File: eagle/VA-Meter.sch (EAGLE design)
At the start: 23 parts, among them IC1 MEGA328P, IC2 7805TV

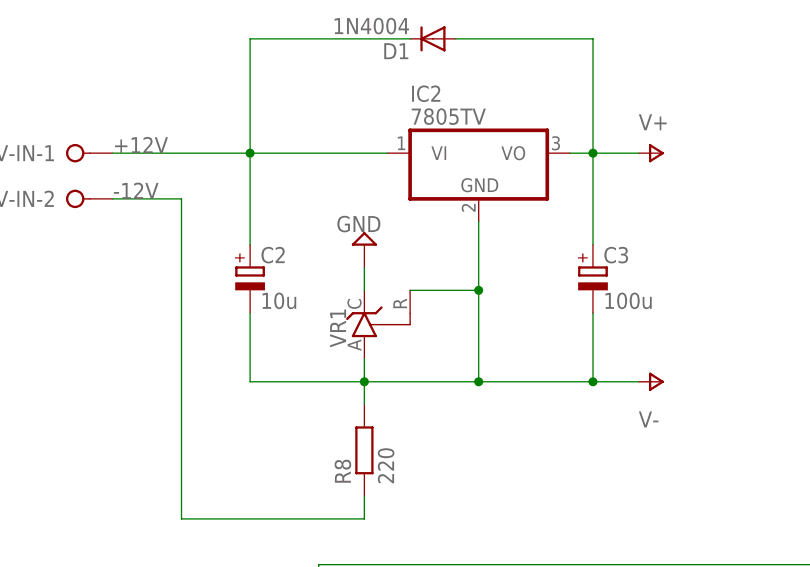
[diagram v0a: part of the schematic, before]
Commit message: 回路図を修正　シャントレギュレータの接続
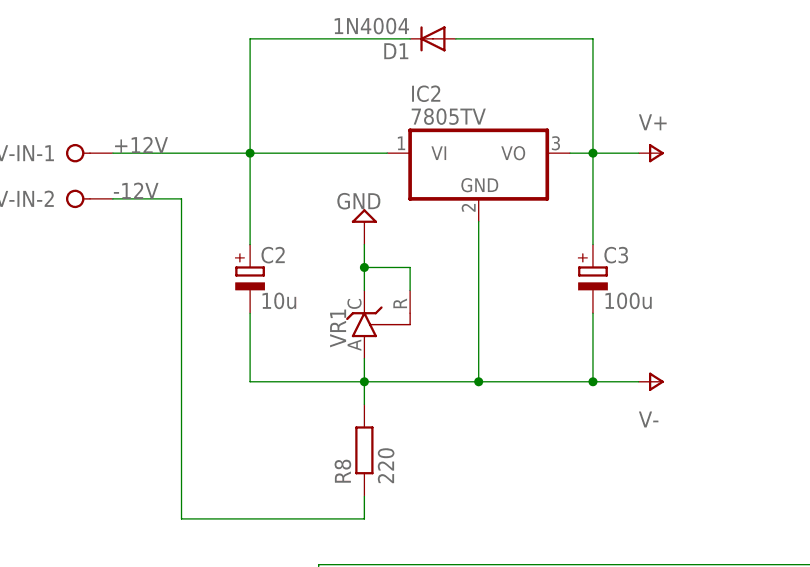
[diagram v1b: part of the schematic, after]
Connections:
- net GND: now also VR1.R
- net V-: no longer VR1.R
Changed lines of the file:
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@@
 <setting verticaltext="up"/>
 </settings>
-<grid distance="0.1" unitdist="inch" unit="inch" style="dots" multiple="1" display="yes" altdistance="0.01" altunitdist="inch" altunit="inch"/>
+<grid distance="0.1" unitdist="inch" unit="inch" style="lines" multiple="1" display="yes" altdistance="0.01" altunitdist="inch" altunit="inch"/>
 <layers>
-<layer number="1" name="Top" color="4" fill="1" visible="yes" active="no"/>
-<layer number="16" name="Bottom" color="1" fill="1" visible="yes" active="no"/>
-<layer number="17" name="Pads" color="2" fill="1" visible="yes" active="no"/>
-<layer number="18" name="Vias" color="2" fill="1" visible="yes" active="no"/>
-<layer number="19" name="Unrouted" color="6" fill="1" visible="yes" active="no"/>
-<layer number="20" name="Dimension" color="15" fill="1" visible="yes" active="no"/>
-<layer number="21" name="tPlace" color="7" fill="1" visible="yes" active="no"/>
-<layer number="22" name="bPlace" color="7" fill="1" visible="yes" active="no"/>
-<layer number="23" name="tOrigins" color="15" fill="1" visible="yes" active="no"/>
-<layer number="24" name="bOrigins" color="15" fill="1" visible="yes" active="no"/>
-<layer number="25" name="tNames" color="7" fill="1" visible="yes" active="no"/>
-<layer number="26" name="bNames" color="7" fill="1" visible="yes" active="no"/>
-<layer number="27" name="tValues" color="7" fill="1" visible="yes" active="no"/>
-<layer number="28" name="bValues" color="7" fill="1" visible="yes" active="no"/>
+<layer number="1" name="Top" color="4" fill="1" visible="no" active="no"/>
+<layer number="16" name="Bottom" color="1" fill="1" visible="no" active="no"/>
+<layer number="17" name="Pads" color="2" fill="1" visible="no" active="no"/>
+<layer number="18" name="Vias" color="2" fill="1" visible="no" active="no"/>
+<layer number="19" name="Unrouted" color="6" fill="1" visible="no" active="no"/>
+<layer number="20" name="Dimension" color="15" fill="1" visible="no" active="no"/>
+<layer number="21" name="tPlace" color="7" fill="1" visible="no" active="no"/>
+<layer number="22" name="bPlace" color="7" fill="1" visible="no" active="no"/>
+<layer number="23" name="tOrigins" color="15" fill="1" visible="no" active="no"/>
+<layer number="24" name="bOrigins" color="15" fill="1" visible="no" active="no"/>
+<layer number="25" name="tNames" color="7" fill="1" visible="no" active="no"/>
+<layer number="26" name="bNames" color="7" fill="1" visible="no" active="no"/>
+<layer number="27" name="tValues" color="7" fill="1" visible="no" active="no"/>
+<layer number="28" name="bValues" color="7" fill="1" visible="no" active="no"/>
 <layer number="29" name="tStop" color="7" fill="3" visible="no" active="no"/>
 <layer number="30" name="bStop" color="7" fill="6" visible="no" active="no"/>
@@
 <layer number="35" name="tGlue" color="7" fill="4" visible="no" active="no"/>
 <layer number="36" name="bGlue" color="7" fill="5" visible="no" active="no"/>
-<layer number="37" name="tTest" color="7" fill="1" visible="yes" active="no"/>
-<layer number="38" name="bTest" color="7" fill="1" visible="yes" active="no"/>
+<layer number="37" name="tTest" color="7" fill="1" visible="no" active="no"/>
+<layer number="38" name="bTest" color="7" fill="1" visible="no" active="no"/>
 <layer number="39" name="tKeepout" color="4" fill="11" visible="no" active="no"/>
 <layer number="40" name="bKeepout" color="1" fill="11" visible="no" active="no"/>
@@
 <layer number="44" name="Drills" color="7" fill="1" visible="no" active="no"/>
 <layer number="45" name="Holes" color="7" fill="1" visible="no" active="no"/>
-<layer number="46" name="Milling" color="3" fill="1" visible="yes" active="no"/>
-<layer number="47" name="Measures" color="7" fill="1" visible="yes" active="no"/>
-<layer number="48" name="Document" color="7" fill="1" visible="yes" active="no"/>
-<layer number="49" name="Reference" color="7" fill="1" visible="yes" active="no"/>
-<layer number="51" name="tDocu" color="6" fill="9" visible="yes" active="no"/>
-<layer number="52" name="bDocu" color="7" fill="1" visible="yes" active="no"/>
+<layer number="46" name="Milling" color="3" fill="1" visible="no" active="no"/>
+<layer number="47" name="Measures" color="7" fill="1" visible="no" active="no"/>
+<layer number="48" name="Document" color="7" fill="1" visible="no" active="no"/>
+<layer number="49" name="Reference" color="7" fill="1" visible="no" active="no"/>
+<layer number="51" name="tDocu" color="6" fill="9" visible="no" active="no"/>
+<layer number="52" name="bDocu" color="7" fill="1" visible="no" active="no"/>
 <layer number="91" name="Nets" color="2" fill="1" visible="yes" active="yes"/>
 <layer number="92" name="Busses" color="1" fill="1" visible="yes" active="yes"/>
@@
 <instance part="VR1" gate="G$1" x="20.32" y="137.16" rot="MR90"/>
 <instance part="R8" gate="G$1" x="20.32" y="121.92" rot="R90"/>
-<instance part="SUPPLY4" gate="GND" x="20.32" y="144.78" rot="R180"/>
+<instance part="SUPPLY4" gate="GND" x="20.32" y="147.32" rot="R180"/>
 <instance part="GND" gate="-1" x="-5.08" y="71.12"/>
 <instance part="GND" gate="-2" x="-5.08" y="66.04"/>
@@
 <pinref part="VR1" gate="G$1" pin="C"/>
 <pinref part="SUPPLY4" gate="GND" pin="GND"/>
+<wire x1="20.32" y1="144.78" x2="20.32" y2="142.24" width="0.1524" layer="91"/>
 <wire x1="20.32" y1="142.24" x2="20.32" y2="139.7" width="0.1524" layer="91"/>
+<wire x1="20.32" y1="142.24" x2="25.4" y2="142.24" width="0.1524" layer="91"/>
+<junction x="20.32" y="142.24"/>
+<pinref part="VR1" gate="G$1" pin="R"/>
+<wire x1="25.4" y1="142.24" x2="25.4" y2="139.7" width="0.1524" layer="91"/>
 </segment>
 <segment>
@@
 <junction x="20.32" y="129.54"/>
 <pinref part="IC2" gate="A1" pin="GND"/>
-<wire x1="33.02" y1="129.54" x2="33.02" y2="139.7" width="0.1524" layer="91"/>
-<pinref part="VR1" gate="G$1" pin="R"/>
-<wire x1="33.02" y1="139.7" x2="33.02" y2="147.32" width="0.1524" layer="91"/>
-<wire x1="25.4" y1="139.7" x2="33.02" y2="139.7" width="0.1524" layer="91"/>
-<junction x="33.02" y="139.7"/>
+<wire x1="33.02" y1="129.54" x2="33.02" y2="147.32" width="0.1524" layer="91"/>
 <wire x1="20.32" y1="129.54" x2="7.62" y2="129.54" width="0.1524" layer="91"/>
 <pinref part="C2" gate="G$1" pin="-"/>

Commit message: 回路図修正
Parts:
- added R11: 1k, rcl:R-EU_0613/15
- D1: value 1N4004 -> 1S2; device diode:1N4004 -> diode:SCHOTTKY-DIODECB417-15
- R8: value 220 -> 3.3k
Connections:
- new net N$1: R11.1
- net -12V: now also R11.2
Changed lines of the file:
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@@
 <setting verticaltext="up"/>
 </settings>
-<grid distance="0.1" unitdist="inch" unit="inch" style="lines" multiple="1" display="yes" altdistance="0.01" altunitdist="inch" altunit="inch"/>
+<grid distance="0.1" unitdist="inch" unit="inch" style="lines" multiple="1" display="no" altdistance="0.01" altunitdist="inch" altunit="inch"/>
 <layers>
 <layer number="1" name="Top" color="4" fill="1" visible="no" active="no"/>
@@
 <part name="IC2" library="linear" deviceset="78*" device="TV" technology="05"/>
 <part name="VR1" library="v-reg" deviceset="TL431CLP" device=""/>
-<part name="R8" library="rcl" deviceset="R-EU_" device="0613/15" value="220"/>
+<part name="R8" library="rcl" deviceset="R-EU_" device="0613/15" value="3.3k"/>
 <part name="SUPPLY4" library="supply2" deviceset="GND" device=""/>
 <part name="GND" library="con-wago-508" deviceset="W237-03P" device=""/>
@@
 <part name="JP2" library="pinhead" deviceset="PINHD-1X2" device=""/>
 <part name="FRAME1" library="frames" deviceset="A4L-LOC" device=""/>
-<part name="D1" library="diode" deviceset="1N4004" device=""/>
+<part name="R11" library="rcl" deviceset="R-EU_" device="0613/15" value="1k"/>
+<part name="SUPPLY6" library="supply2" deviceset="GND" device=""/>
+<part name="D1" library="diode" deviceset="SCHOTTKY-DIODE" device="CB417-15" value="1S2"/>
 </parts>
 <sheets>
@@
 <instance part="JP2" gate="G$1" x="-17.78" y="104.14" rot="R180"/>
 <instance part="FRAME1" gate="G$1" x="-43.18" y="7.62"/>
-<instance part="D1" gate="1" x="27.94" y="167.64" rot="R180"/>
+<instance part="R11" gate="G$1" x="33.02" y="114.3" rot="R180"/>
+<instance part="SUPPLY6" gate="GND" x="45.72" y="114.3" rot="R90"/>
+<instance part="D1" gate="G$1" x="27.94" y="167.64" rot="R180"/>
 </instances>
 <busses>
@@
 <wire x1="-7.62" y1="154.94" x2="7.62" y2="154.94" width="0.1524" layer="91"/>
 <label x="-7.62" y="154.94" size="1.778" layer="95"/>
-<pinref part="D1" gate="1" pin="C"/>
 <wire x1="25.4" y1="167.64" x2="7.62" y2="167.64" width="0.1524" layer="91"/>
 <wire x1="7.62" y1="167.64" x2="7.62" y2="154.94" width="0.1524" layer="91"/>
+<pinref part="D1" gate="G$1" pin="C"/>
 </segment>
 </net>
@@
 <wire x1="45.72" y1="154.94" x2="45.72" y2="167.64" width="0.1524" layer="91"/>
 <wire x1="45.72" y1="167.64" x2="30.48" y2="167.64" width="0.1524" layer="91"/>
-<pinref part="D1" gate="1" pin="A"/>
+<pinref part="D1" gate="G$1" pin="A"/>
 </segment>
 <segment>
@@
 <wire x1="0" y1="149.86" x2="0" y2="114.3" width="0.1524" layer="91"/>
 <label x="-7.62" y="149.86" size="1.778" layer="95"/>
+<pinref part="R11" gate="G$1" pin="2"/>
+<wire x1="27.94" y1="114.3" x2="20.32" y2="114.3" width="0.1524" layer="91"/>
+<junction x="20.32" y="114.3"/>
 </segment>
 </net>
@@
 </segment>
 </net>
+<net name="N$1" class="0">
+<segment>
+<pinref part="R11" gate="G$1" pin="1"/>
+<wire x1="38.1" y1="114.3" x2="45.72" y2="114.3" width="0.1524" layer="91"/>
+</segment>
+</net>
